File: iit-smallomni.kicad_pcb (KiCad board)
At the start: 2 copper layers, 100 x 100 mm, 88 parts, among them J1 Battery, J10 DC-Motor, J11 Conn_02x05_Odd_Even, J12 LiPo guard, J2 HC_SR04, J3 HC_SR04, J4 HC_SR04, J5 DC-Motor, J6 DC-Motor, J7 DC-Motor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

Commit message: All routed except GND
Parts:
- moved R4 5.10 mm to (181.9, 52.8), turned to 0 degrees
- moved R9 4.15 mm to (181.6, 67.1), turned to 0 degrees
- moved R3 3.70 mm to (177.8, 52.8), turned to 0 degrees
- moved C6 2.87 mm to (217.9, 42.7)
- moved R31 2.86 mm to (166.2, 59.9)
- moved J9 2.09 mm to (161.6, 73.6)
- moved C8 0.51 mm to (221.0, 69.6)
- moved R8 0.36 mm to (237.5, 75.9)
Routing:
- net +3.3V: track 280.9 -> 548.6 mm, vias 1 -> 2
- net +5V: track 58.8 -> 205.7 mm, vias 0 -> 4
- net VCC: track 39.0 -> 136.6 mm, vias 0 -> 4
- net /UV_Trig_3: track 6.15 -> 95.7 mm, vias 0 -> 4
- net /MPU95 interrupt: track 0.00 -> 53.9 mm, vias 0 -> 2
- net /JTAG_TDO: track 32.3 -> 86.0 mm, vias 0 -> 2
- net /JTAG_TDI: track 54.6 -> 99.0 mm
- net /Mot2_B: track 0.00 -> 39.1 mm
- net /Mot2_A: track 0.00 -> 38.8 mm
- net /JTAG_TCK: track 65.1 -> 96.4 mm
- net /Battery level: track 53.8 -> 81.1 mm
- net /JTAG_TMS: track 58.8 -> 85.2 mm
- net /Mot1_B: track 0.00 -> 25.7 mm, vias 0 -> 1
- net /Mot1_A: track 0.00 -> 25.7 mm
- net /Mot3_A: track 44.4 -> 64.7 mm
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
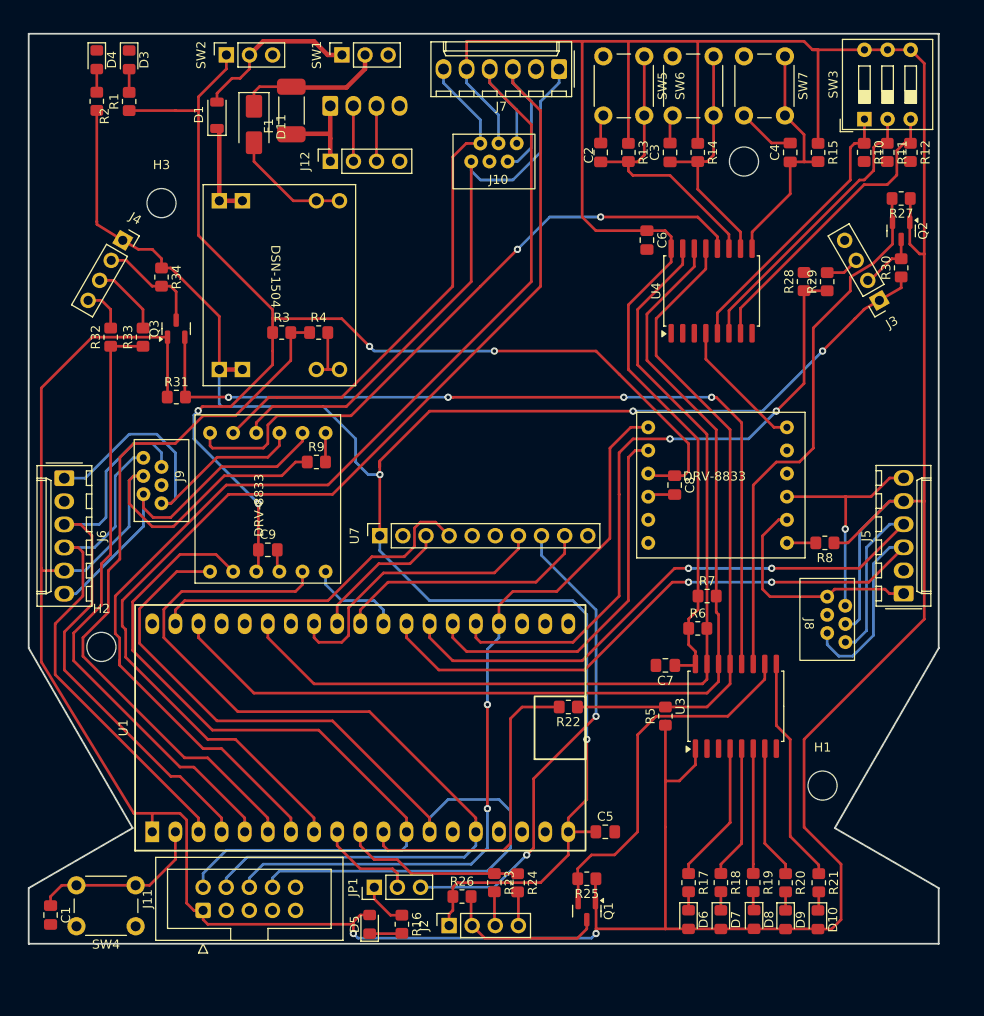
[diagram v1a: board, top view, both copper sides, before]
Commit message: Routing done, ERC & DRC errors eliminated
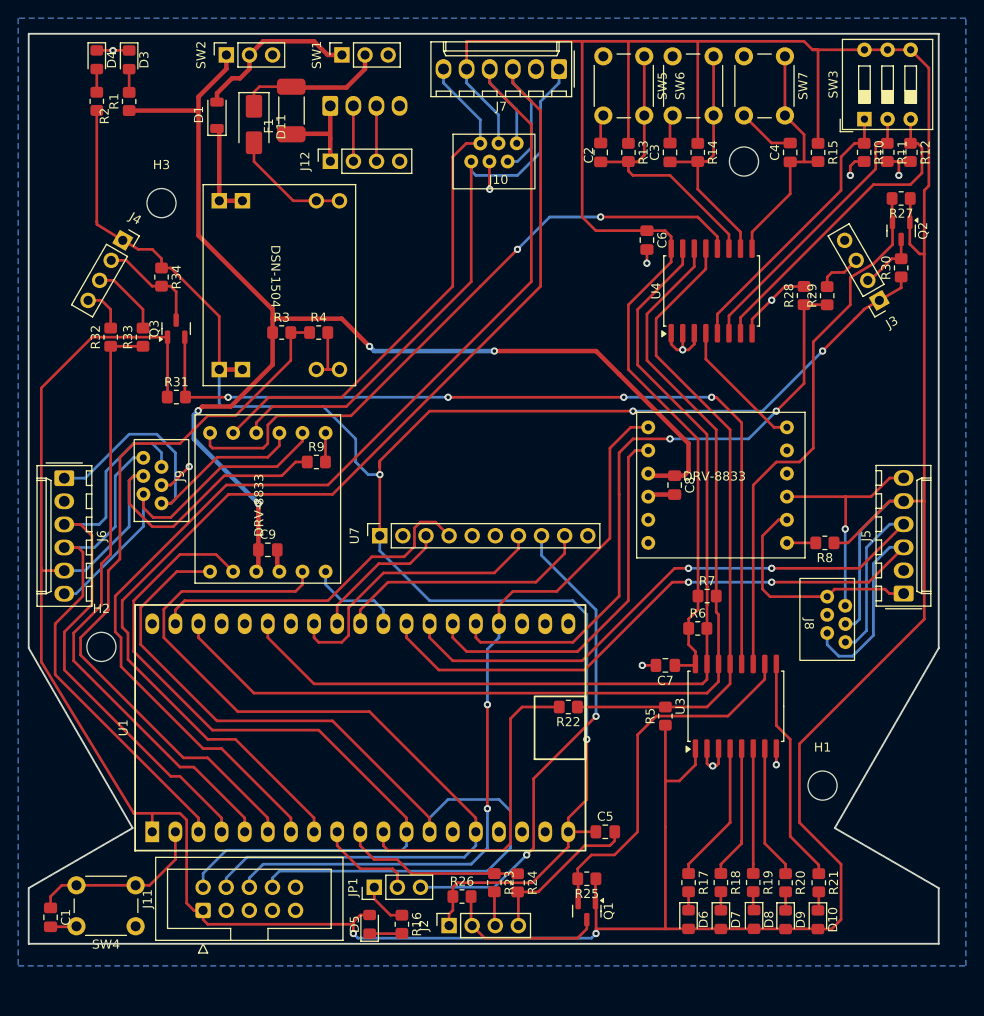
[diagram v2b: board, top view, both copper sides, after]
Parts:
- moved R28 1.54 mm to (235.2, 48.8)
- moved R29 1.54 mm to (237.7, 48.8)
- moved C1 0.25 mm to (152.4, 117.1)
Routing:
- net GND: track 46.7 -> 106.5 mm, vias 0 -> 11
- net Net-(U4-P3): track 33.2 -> 35.2 mm
- net /UV_Echo_2: track 71.6 -> 70.0 mm
- net Net-(J3-Pin_3): track 3.75 -> 4.94 mm
- net +3.3V: track 548.6 -> 549.4 mm
- net +5V: track 205.7 -> 205.2 mm
- added copper zone on B.Cu, net GND

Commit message: JTAG signal naming fixed
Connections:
- net /JTAG_TCK renamed /Mot3_DrvA-JTAG_TCK
- net /JTAG_TDI renamed /Mot2_DrvB-JTAG_TDI
- net /JTAG_TDO renamed /Mot1_DrvA-JTAG_TDO
- net /JTAG_TMS renamed /Mot2_DrvA-JTAG_TMS

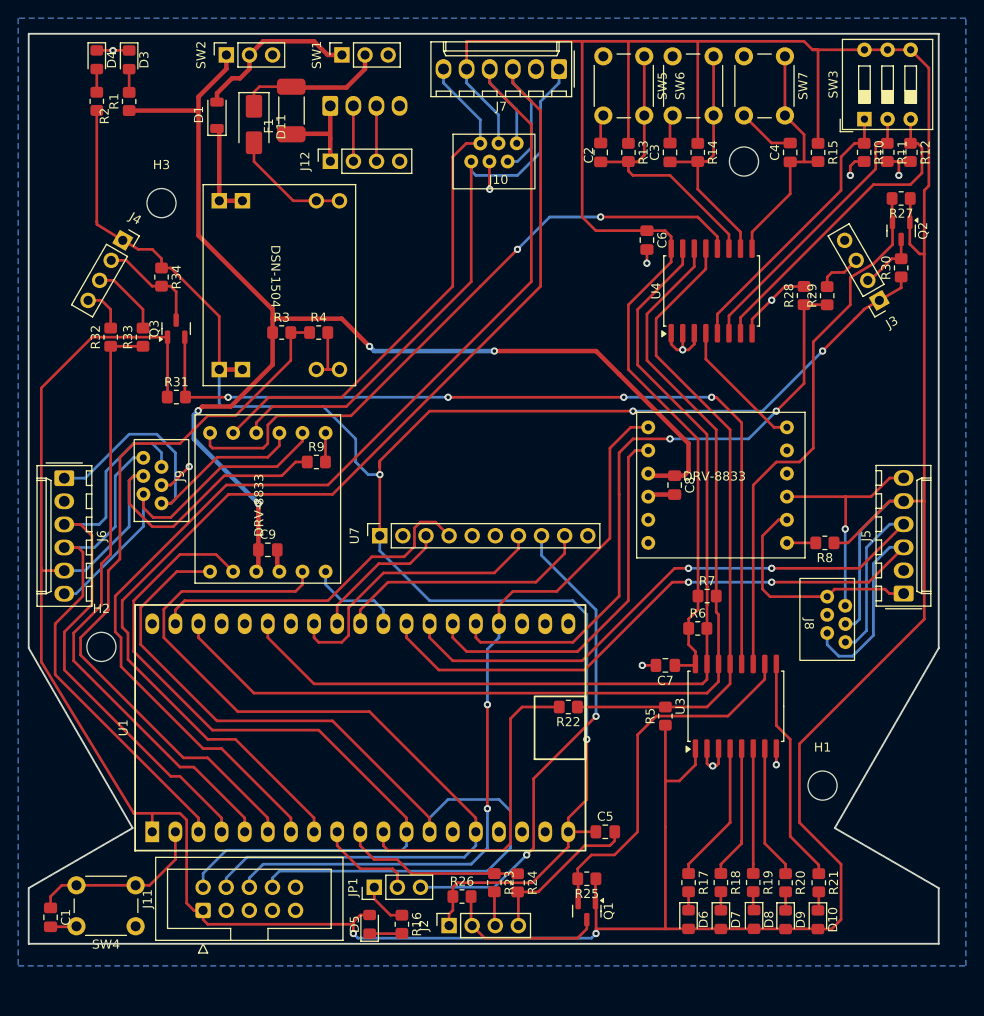
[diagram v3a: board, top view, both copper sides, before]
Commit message: Tidy up silkscreen, eliminate warnings
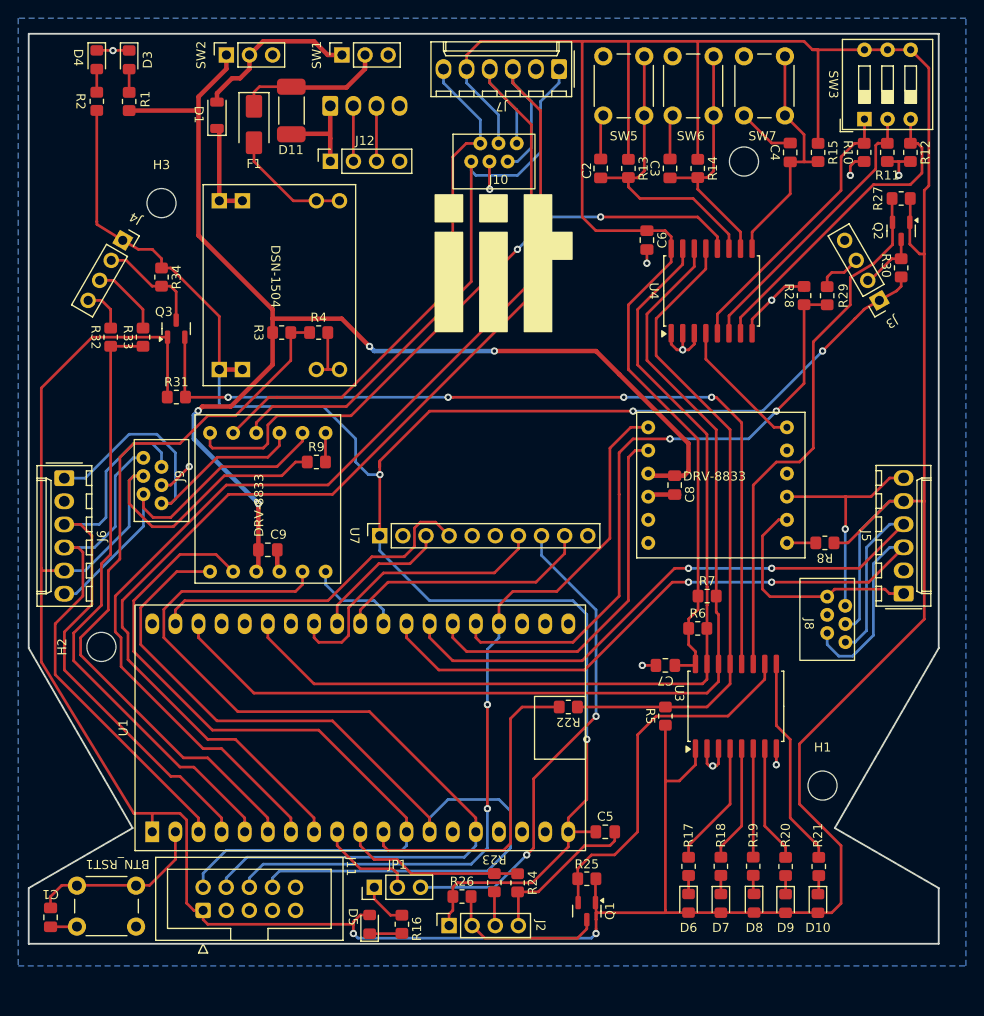
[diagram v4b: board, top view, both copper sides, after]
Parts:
- removed SW4: SW_Push, Button_Switch_THT:SW_PUSH_6mm_H5mm
- added BTN_RST1: SW_Push, Button_Switch_THT:SW_PUSH_6mm_H5mm, F.Cu at (161.8, 118.1)
- added G***: LOGO, iit-smallomni:IIT_logo_15x15mm, F.Cu at (202.2, 45.2)
- moved D10 1.79 mm to (236.7, 115.6)
- moved D9 1.79 mm to (233.2, 115.6)
- moved R18 1.79 mm to (226.1, 111.5)
- moved R19 1.79 mm to (229.6, 111.5)
- moved R20 1.79 mm to (233.2, 111.5)
- moved R21 1.79 mm to (236.8, 111.5)
- moved D6 1.79 mm to (222.5, 115.6)
- moved D7 1.79 mm to (226.1, 115.6)
- moved D8 1.79 mm to (229.7, 115.5)
- moved R17 1.79 mm to (222.5, 111.5)
- moved C2 1.76 mm to (212.9, 34.8)
- moved C3 1.76 mm to (220.5, 34.8)
- moved R13 1.76 mm to (215.9, 34.8)
- moved R14 1.76 mm to (223.5, 34.8)
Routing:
- net GND: track 106.5 -> 110.0 mm
- net /LED_5: track 25.0 -> 23.2 mm
- net /LED_3: track 13.7 -> 11.9 mm
- net /LED_4: track 14.7 -> 12.9 mm
- net /LED_2: track 14.7 -> 12.9 mm
- net /LED_1: track 15.6 -> 13.8 mm
- net /Button_1: track 32.0 -> 33.0 mm
- net +3.3V: track 549.4 -> 548.8 mm
- net +5V: track 205.2 -> 205.8 mm

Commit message: Add pin annotations
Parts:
- moved G*** 6.20 mm to (205.7, 50.3)
- moved R8 0.25 mm to (237.2, 75.9)
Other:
- board text added: "+"
- board text added: "+12V"
- board text added: "+3v3"
- board text added: "+5V"
- board text added: "-"
- board text added: "1A"
- board text added: "1B"
- board text added: "2A"
- board text added: "2B"
- board text added: "3A"
- board text added: "3B"
- board text added: "3v3"
- board text added: "ECL"
- board text added: "EDA"
- board text added: "Echo"
- board text added: "EncA"
- board text added: "EncB"
- board text added: "FT"
- board text added: "Fsync"
- board text added: "GND"
- board text added: "Heart"
- board text added: "IIT Robotcsapat Robot alaplap v1.1 Izsó András 2025"
- board text added: "Int"
- board text added: "LiPo guard"
- board text added: "M1A"
- board text added: "M1B"
- board text added: "M2A"
- board text added: "M3A"
- board text added: "M3B"
- board text added: "MA"
- board text added: "MB"
- board text added: "MB 3v3 eB MA GND eA"
- board text added: "MISO"
- board text added: "MOSI"
- board text added: "MOT"
- board text added: "MPU-9250"
- board text added: "M_int"
- board text added: "Off"
- board text added: "On"
- board text added: "POW"
- board text added: "S1"
- board text added: "S2"
- board text added: "S3"
- board text added: "SCLK"
- board text added: "SLEEP"
- board text added: "Trig"
- board text added: "nCS"

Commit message: Add annotation for esp32
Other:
- board text added: "ESP32-NodeMCU32S"
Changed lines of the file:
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@@
+		)
+	)
+	(gr_text "ESP32-NodeMCU32S"
+		(at 187.198 103.632 90)
+		(layer "F.SilkS")
+		(effects
+			(font
+				(size 1 1)
+				(thickness 0.155)
+			)
+			(justify left bottom)
 		)
 	)
